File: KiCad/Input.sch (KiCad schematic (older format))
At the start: 5 parts, among them J1 Conn_01x03, SW1 SW_Push_SPDT

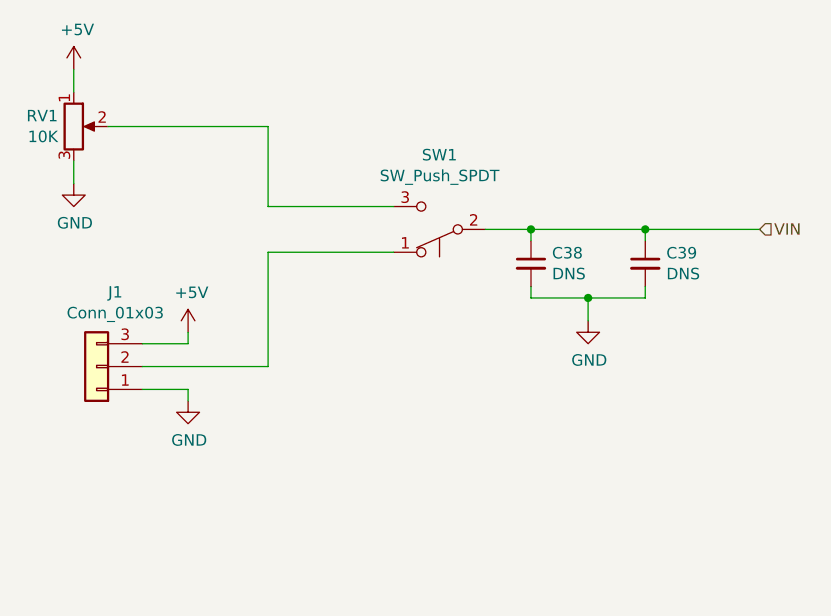
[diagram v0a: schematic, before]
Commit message: Schematic Update First Draft, ERC Passed
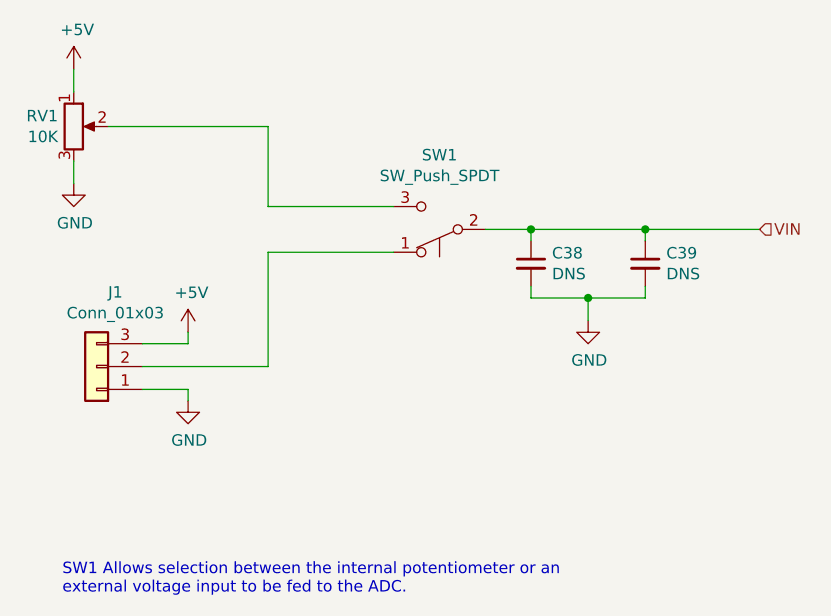
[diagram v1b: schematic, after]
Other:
- note added: "SW1 Allows selection between the internal potentiometer or an\nexternal voltage input to be fed to the ADC."
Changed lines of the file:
@@
 $Descr A4 11693 8268
 encoding utf-8
-Sheet 9 11
+Sheet 9 9
 Title "Schilk_SA-ADC"
 Date "2020-02-03"
@@
 Text HLabel 6200 3450 2    50   Input ~ 0
 VIN
+Text Notes 3150 5050 0    50   ~ 0
+SW1 Allows selection between the internal potentiometer or an\nexternal voltage input to be fed to the ADC.
 $EndSCHEMATC

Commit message: PCB v0.2.
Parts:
- J1: value Conn_01x03 -> Vin
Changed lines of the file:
@@
 $Descr A4 11693 8268
 encoding utf-8
-Sheet 9 9
+Sheet 8 9
 Title "Schilk_SA-ADC"
 Date "2020-02-03"
@@
 P 3300 4050
 F 0 "J1" H 3218 3725 50  0000 C CNN
-F 1 "Conn_01x03" H 3218 3816 50  0000 C CNN
+F 1 "Vin" H 3218 3816 50  0000 C CNN
 F 2 "Connector_PinHeader_2.54mm:PinHeader_1x03_P2.54mm_Vertical" H 3300 4050 50  0001 C CNN
 F 3 "~" H 3300 4050 50  0001 C CNN
